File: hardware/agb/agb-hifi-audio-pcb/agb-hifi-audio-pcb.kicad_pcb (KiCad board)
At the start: 4 copper layers, 25.3 x 35.1 mm, 66 parts, among them J1 TC2030-IDC-NL, J5 SPK+, J6 SPK-, J7 EXPANSION0, J8 EXPANSION1, U1 ESP32-PICO-MINI-02-N8R2, U2 ES8388, U3 TPS61021ADSGR, U4 PAM8302AASCR, U5 LP5907MFX-3.0

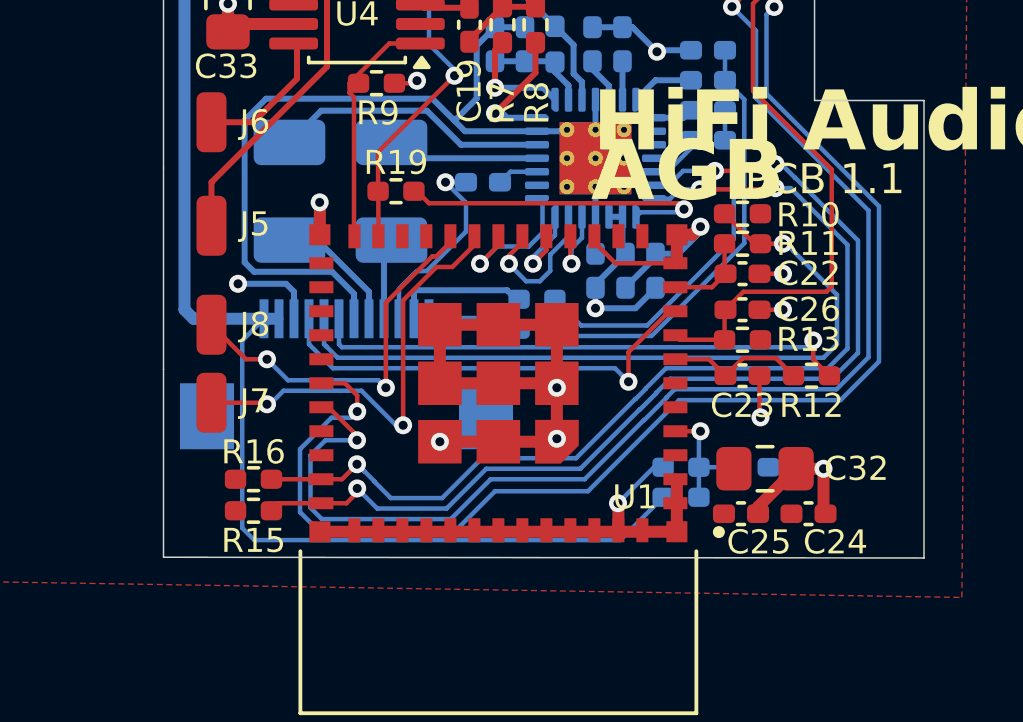
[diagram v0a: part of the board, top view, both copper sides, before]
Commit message: hardware(agb): switch FPC1 to JUSHUO AFC07-S12ECA-00
The Hirose FH12A-12S-0.5SH(55) is out of stock at JLCPCB/LCSC (2 pcs left),
which blocks assembly. Replace it with the JUSHUO AFC07-S12ECA-00 (LCSC
C262585, ~19k stock): same 12-pos 0.5mm top-contact ZIF at the same 2.0mm
height, and the flex tail meets its mating spec (0.3mm thickness, 3.5mm
exposure vs 3.0 minimum, 6.5mm width).

Not a drop-in: the AFC07 fitting nails sit 2.26mm from the pin row vs the
Hirose's 3.25mm, on top of the old VOL/SW/PAIR and VBAT fanout channel, so
those nets are rerouted around the new nail lands. Pin row and net order are
unchanged; the flex geometry is untouched. DRC is clean (0 unconnected, no
live violations).

Footprint and STEP/WRL models are the official JLC library assets (imported
via easyeda2kicad) added to project_footprints. Schematic carries the new
MPN/LCSC/datasheet; the Hirose remains noted as a mate-compatible repair part
for pre-1.1 boards only. Docs updated to match.
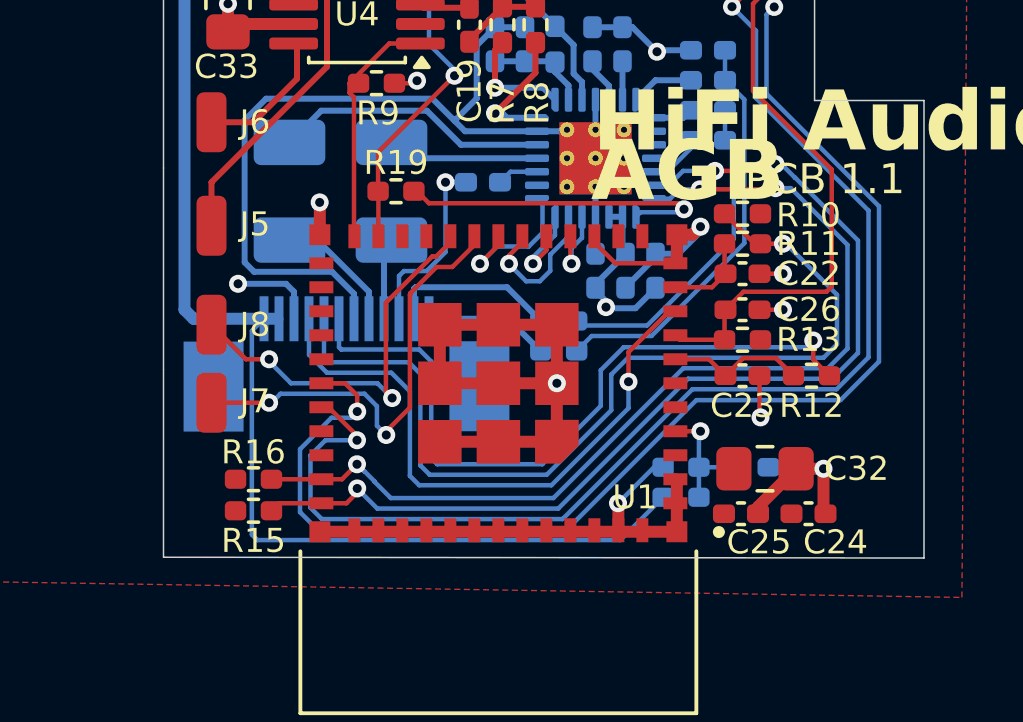
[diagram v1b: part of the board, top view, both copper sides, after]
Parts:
- FPC1: value FH12A-12S-0.5SH(55) -> AFC07-S12ECA-00; footprint project_footprints:HIROSE_FH12A-12S-0.5SH_55_ -> project_footprints:FPC-SMD_12P-P0.50_AFC07-S12ECA-00
- moved FPC1 1.13 mm to (97.0, 119.6)
- moved R3 1.03 mm to (104.1, 119.5)
- moved R4 1.03 mm to (104.1, 118.5)
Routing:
- net SW: track 24.6 -> 30.6 mm
- net VOL: track 18.2 -> 24.1 mm
- net PAIR: track 14.9 -> 20.2 mm
- net Net-(C14-Pad1): track 11.9 -> 10.7 mm
- net LIN: track 4.59 -> 5.71 mm
- net RIN: track 3.21 -> 4.16 mm
- net EXP1: track 12.5 -> 13.3 mm
- net GND: track 90.4 -> 90.1 mm, vias 25 -> 23
